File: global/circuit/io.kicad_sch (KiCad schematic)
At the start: 15 parts

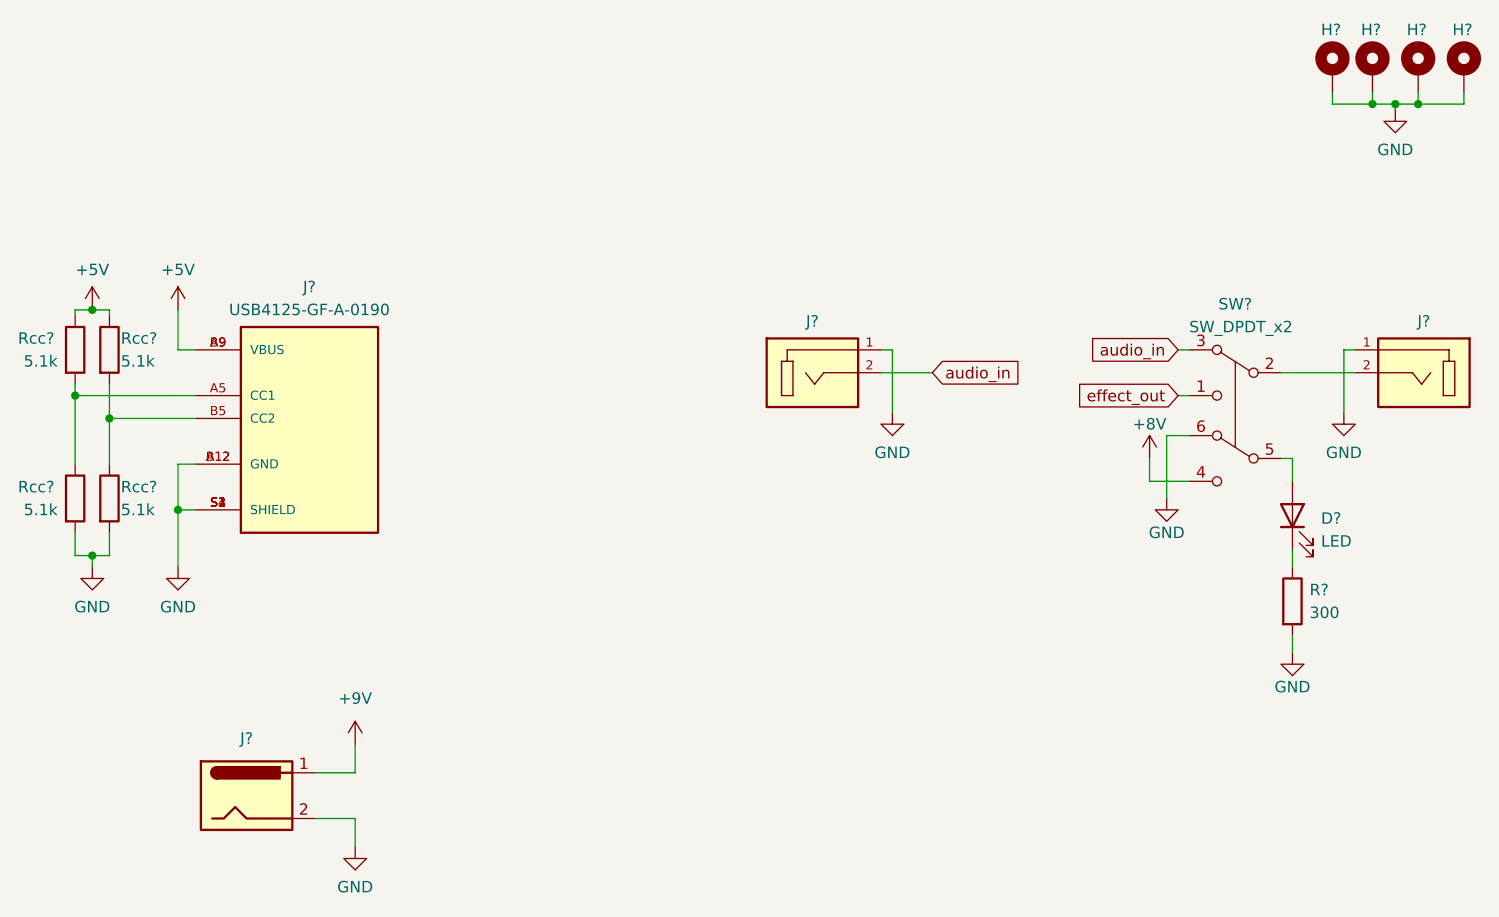
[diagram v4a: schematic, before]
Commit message: minor circuit rework for better use with multiple projects
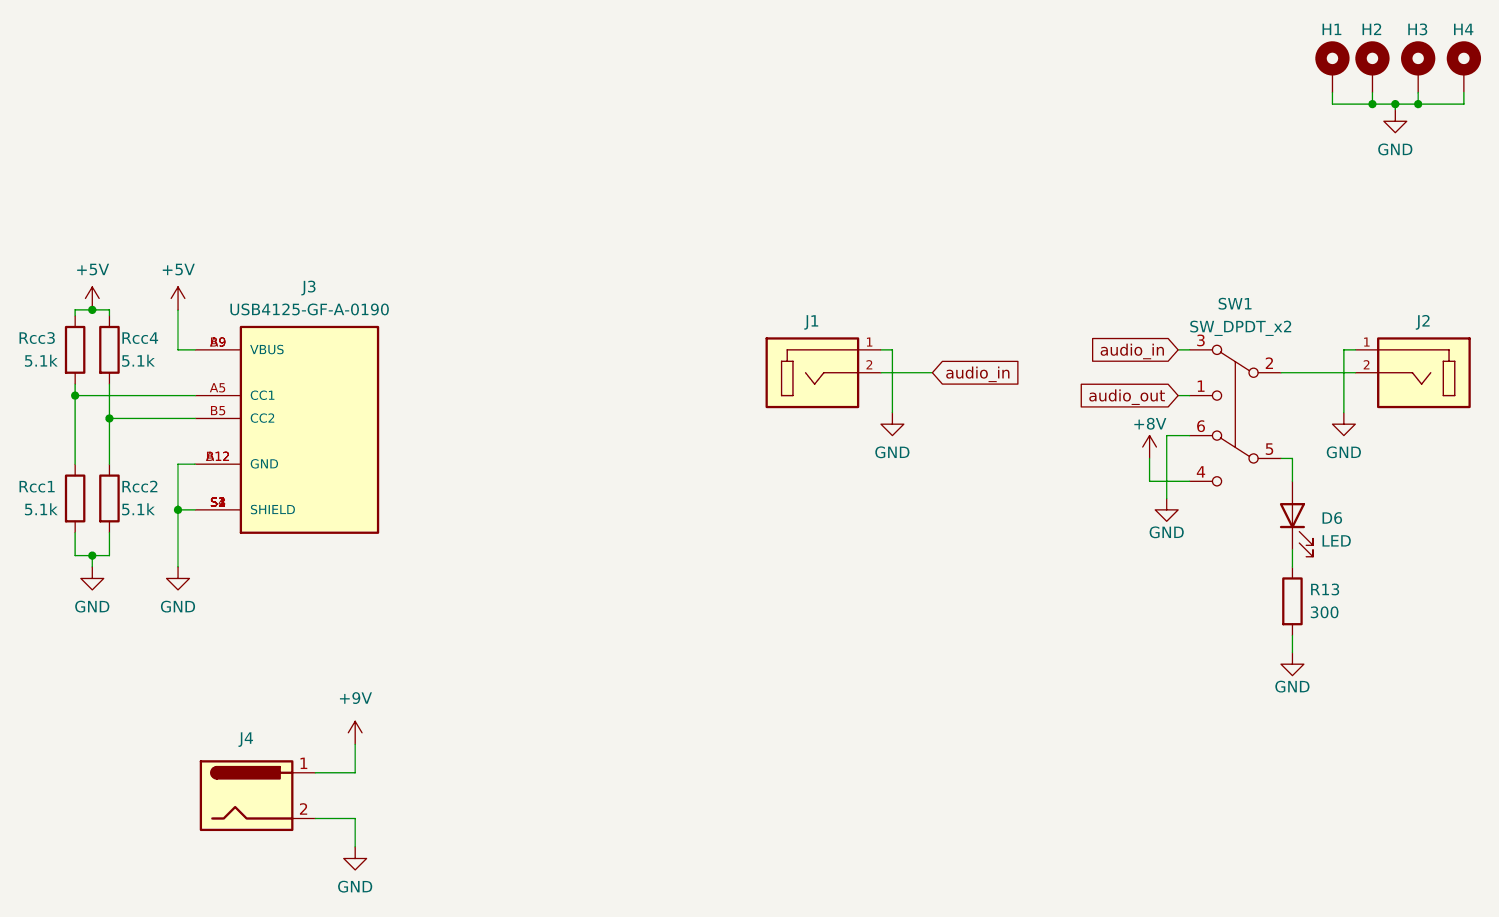
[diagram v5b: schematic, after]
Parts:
- J2: renamed from J?; footprint effect_pedal:audio_jack_wired -> effect_pedal:audio_jack_wired_shield_only
- J4: renamed from J?; footprint effect_pedal:barrel_jack_wired -> Connector_PinHeader_2.54mm:PinHeader_1x02_P2.54mm_Vertical
- SW1: renamed from SW?; footprint effect_pedal:switch_wired -> effect_pedal:switch_wired_reduced
- gave numbers to parts that had none: 12
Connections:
- net effect_out renamed audio_out
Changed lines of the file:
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@@
     )
   )
-  (global_label "effect_out" (shape input) (at 151.765 58.42 180) (fields_autoplaced)
+  (global_label "audio_out" (shape input) (at 151.765 58.42 180) (fields_autoplaced)
     (effects (font (size 1.27 1.27)) (justify right))
-    (property "Intersheet References" "${INTERSHEET_REFS}" (id 0) (at 139.9176 58.3406 0)
+    (property "Intersheet References" "${INTERSHEET_REFS}" (id 0) (at 140.1595 58.3406 0)
       (effects (font (size 1.27 1.27)) (justify right) hide)
     )
@@
   (symbol (lib_id "power:GND") (at 120.015 60.325 0) (unit 1)
     (in_bom yes) (on_board yes)
-    (property "Reference" "#PWR?" (id 0) (at 120.015 66.675 0)
+    (property "Reference" "#PWR0109" (id 0) (at 120.015 66.675 0)
       (effects (font (size 1.27 1.27)) hide)
     )
@@
   (symbol (lib_id "power:GND") (at 150.495 69.85 0) (unit 1)
     (in_bom yes) (on_board yes)
-    (property "Reference" "#PWR?" (id 0) (at 150.495 76.2 0)
+    (property "Reference" "#PWR026" (id 0) (at 150.495 76.2 0)
       (effects (font (size 1.27 1.27)) hide)
     )
@@
   (symbol (lib_id "power:+5V") (at 31.115 48.895 0) (unit 1)
     (in_bom yes) (on_board yes)
-    (property "Reference" "#PWR?" (id 0) (at 31.115 52.705 0)
+    (property "Reference" "#PWR028" (id 0) (at 31.115 52.705 0)
       (effects (font (size 1.27 1.27)) hide)
     )
@@
   (symbol (lib_id "Connector:Barrel_Jack") (at 48.26 102.87 0) (unit 1)
     (in_bom yes) (on_board yes)
-    (property "Reference" "J?" (id 0) (at 48.26 96.52 0))
+    (property "Reference" "J4" (id 0) (at 48.26 96.52 0))
     (property "Value" "Barrel_Jack" (id 1) (at 48.26 96.52 0)
       (effects (font (size 1.27 1.27)) hide)
     )
-    (property "Footprint" "effect_pedal:barrel_jack_wired" (id 2) (at 49.53 103.886 0)
+    (property "Footprint" "Connector_PinHeader_2.54mm:PinHeader_1x02_P2.54mm_Vertical" (id 2) (at 49.53 103.886 0)
       (effects (font (size 1.27 1.27)) hide)
     )
@@
   (symbol (lib_id "Device:R") (at 33.02 53.34 0) (unit 1)
     (in_bom yes) (on_board yes)
-    (property "Reference" "Rcc?" (id 0) (at 34.29 52.07 0)
+    (property "Reference" "Rcc4" (id 0) (at 34.29 52.07 0)
       (effects (font (size 1.27 1.27)) (justify left))
     )
@@
   (symbol (lib_id "power:GND") (at 40.64 77.47 0) (unit 1)
     (in_bom yes) (on_board yes)
-    (property "Reference" "#PWR?" (id 0) (at 40.64 83.82 0)
+    (property "Reference" "#PWR0113" (id 0) (at 40.64 83.82 0)
       (effects (font (size 1.27 1.27)) hide)
     )
@@
   (symbol (lib_id "power:+9V") (at 60.325 97.155 0) (unit 1)
     (in_bom yes) (on_board yes) (fields_autoplaced)
-    (property "Reference" "#PWR?" (id 0) (at 60.325 100.965 0)
+    (property "Reference" "#PWR0101" (id 0) (at 60.325 100.965 0)
       (effects (font (size 1.27 1.27)) hide)
     )
@@
   (symbol (lib_id "Mechanical:MountingHole_Pad") (at 178.435 22.225 0) (unit 1)
     (in_bom yes) (on_board yes)
-    (property "Reference" "H?" (id 0) (at 177.165 17.78 0)
+    (property "Reference" "H3" (id 0) (at 177.165 17.78 0)
       (effects (font (size 1.27 1.27)) (justify left))
     )
@@
   (symbol (lib_id "power:GND") (at 170.18 60.325 0) (unit 1)
     (in_bom yes) (on_board yes)
-    (property "Reference" "#PWR?" (id 0) (at 170.18 66.675 0)
+    (property "Reference" "#PWR0108" (id 0) (at 170.18 66.675 0)
       (effects (font (size 1.27 1.27)) hide)
     )
@@
   (symbol (lib_id "Device:R") (at 164.465 81.28 0) (unit 1)
     (in_bom yes) (on_board yes) (fields_autoplaced)
-    (property "Reference" "R?" (id 0) (at 166.37 80.0099 0)
+    (property "Reference" "R13" (id 0) (at 166.37 80.0099 0)
       (effects (font (size 1.27 1.27)) (justify left))
     )
@@
   (symbol (lib_id "Mechanical:MountingHole_Pad") (at 183.515 22.225 0) (unit 1)
     (in_bom yes) (on_board yes)
-    (property "Reference" "H?" (id 0) (at 182.245 17.78 0)
+    (property "Reference" "H4" (id 0) (at 182.245 17.78 0)
       (effects (font (size 1.27 1.27)) (justify left))
     )
@@
   (symbol (lib_id "Device:R") (at 29.21 69.85 0) (unit 1)
     (in_bom yes) (on_board yes)
-    (property "Reference" "Rcc?" (id 0) (at 22.86 68.58 0)
+    (property "Reference" "Rcc1" (id 0) (at 22.86 68.58 0)
       (effects (font (size 1.27 1.27)) (justify left))
     )
@@
   (symbol (lib_id "power:+5V") (at 40.64 48.895 0) (unit 1)
     (in_bom yes) (on_board yes)
-    (property "Reference" "#PWR?" (id 0) (at 40.64 52.705 0)
+    (property "Reference" "#PWR0114" (id 0) (at 40.64 52.705 0)
       (effects (font (size 1.27 1.27)) hide)
     )
@@
   (symbol (lib_id "effect_pedal:audio_jack_1_GND") (at 111.125 55.88 0) (unit 1)
     (in_bom yes) (on_board yes)
-    (property "Reference" "J?" (id 0) (at 111.125 50.165 0))
+    (property "Reference" "J1" (id 0) (at 111.125 50.165 0))
     (property "Value" "AudioJack2_Ground" (id 1) (at 110.49 49.53 0)
       (effects (font (size 1.27 1.27)) hide)
@@
   (symbol (lib_id "effect_pedal:USB4125-GF-A-0190_REVA2") (at 55.245 60.96 0) (unit 1)
     (in_bom yes) (on_board yes)
-    (property "Reference" "J?" (id 0) (at 55.245 46.355 0))
+    (property "Reference" "J3" (id 0) (at 55.245 46.355 0))
     (property "Value" "USB4125-GF-A-0190" (id 1) (at 55.245 48.895 0))
     (property "Footprint" "GCT_USB4125-GF-A-0190_REVA2" (id 2) (at 55.245 60.96 0)
@@
   (symbol (lib_id "effect_pedal:audio_jack_1_GND") (at 179.07 55.88 0) (mirror y) (unit 1)
     (in_bom yes) (on_board yes)
-    (property "Reference" "J?" (id 0) (at 179.07 50.165 0))
+    (property "Reference" "J2" (id 0) (at 179.07 50.165 0))
     (property "Value" "AudioJack2_Ground" (id 1) (at 179.705 49.53 0)
       (effects (font (size 1.27 1.27)) hide)
     )
-    (property "Footprint" "effect_pedal:audio_jack_wired" (id 2) (at 179.07 55.88 0)
+    (property "Footprint" "effect_pedal:audio_jack_wired_shield_only" (id 2) (at 179.07 55.88 0)
       (effects (font (size 1.27 1.27)) hide)
     )
@@
   (symbol (lib_id "Mechanical:MountingHole_Pad") (at 168.91 22.225 0) (unit 1)
     (in_bom yes) (on_board yes)
-    (property "Reference" "H?" (id 0) (at 167.64 17.78 0)
+    (property "Reference" "H1" (id 0) (at 167.64 17.78 0)
       (effects (font (size 1.27 1.27)) (justify left))
     )
@@
   (symbol (lib_id "power:GND") (at 31.115 77.47 0) (unit 1)
     (in_bom yes) (on_board yes)
-    (property "Reference" "#PWR?" (id 0) (at 31.115 83.82 0)
+    (property "Reference" "#PWR0112" (id 0) (at 31.115 83.82 0)
       (effects (font (size 1.27 1.27)) hide)
     )
@@
   (symbol (lib_id "power:GND") (at 175.895 26.67 0) (unit 1)
     (in_bom yes) (on_board yes) (fields_autoplaced)
-    (property "Reference" "#PWR?" (id 0) (at 175.895 33.02 0)
+    (property "Reference" "#PWR05" (id 0) (at 175.895 33.02 0)
       (effects (font (size 1.27 1.27)) hide)
     )
@@
   (symbol (lib_id "effect_pedal:SF12011F-0202-20R-L-050") (at 160.02 55.88 0) (mirror y) (unit 1)
     (in_bom yes) (on_board yes)
-    (property "Reference" "SW?" (id 0) (at 158.115 48.26 0))
+    (property "Reference" "SW1" (id 0) (at 158.115 48.26 0))
     (property "Value" "SW_DPDT_x2" (id 1) (at 158.75 50.8 0))
-    (property "Footprint" "effect_pedal:switch_wired" (id 2) (at 133.35 53.34 0)
+    (property "Footprint" "effect_pedal:switch_wired_reduced" (id 2) (at 133.35 53.34 0)
       (effects (font (size 1.27 1.27)) (justify left) hide)
     )
@@
   (symbol (lib_id "power:GND") (at 60.325 108.585 0) (unit 1)
     (in_bom yes) (on_board yes) (fields_autoplaced)
-    (property "Reference" "#PWR?" (id 0) (at 60.325 114.935 0)
+    (property "Reference" "#PWR0105" (id 0) (at 60.325 114.935 0)
       (effects (font (size 1.27 1.27)) hide)
     )
@@
   (symbol (lib_id "power:GND") (at 164.465 86.995 0) (unit 1)
     (in_bom yes) (on_board yes)
-    (property "Reference" "#PWR?" (id 0) (at 164.465 93.345 0)
+    (property "Reference" "#PWR027" (id 0) (at 164.465 93.345 0)
       (effects (font (size 1.27 1.27)) hide)
     )
@@
   (symbol (lib_id "Device:LED") (at 164.465 71.755 90) (unit 1)
     (in_bom yes) (on_board yes) (fields_autoplaced)
-    (property "Reference" "D?" (id 0) (at 167.64 72.0724 90)
+    (property "Reference" "D6" (id 0) (at 167.64 72.0724 90)
       (effects (font (size 1.27 1.27)) (justify right))
     )
@@
   (symbol (lib_id "Mechanical:MountingHole_Pad") (at 173.355 22.225 0) (unit 1)
     (in_bom yes) (on_board yes)
-    (property "Reference" "H?" (id 0) (at 172.085 17.78 0)
+    (property "Reference" "H2" (id 0) (at 172.085 17.78 0)
       (effects (font (size 1.27 1.27)) (justify left))
     )
@@
   (symbol (lib_id "Device:R") (at 33.02 69.85 0) (unit 1)
     (in_bom yes) (on_board yes)
-    (property "Reference" "Rcc?" (id 0) (at 34.29 68.58 0)
+    (property "Reference" "Rcc2" (id 0) (at 34.29 68.58 0)
       (effects (font (size 1.27 1.27)) (justify left))
     )
@@
   (symbol (lib_id "Device:R") (at 29.21 53.34 0) (unit 1)
     (in_bom yes) (on_board yes)
-    (property "Reference" "Rcc?" (id 0) (at 22.86 52.07 0)
+    (property "Reference" "Rcc3" (id 0) (at 22.86 52.07 0)
       (effects (font (size 1.27 1.27)) (justify left))
     )
@@
   (symbol (lib_id "power:+8V") (at 148.59 65.405 0) (unit 1)
     (in_bom yes) (on_board yes)
-    (property "Reference" "#PWR?" (id 0) (at 148.59 69.215 0)
-      (effects (font (size 1.27 1.27)) hide)
-    )
+    (property "Reference" "#PWR025" (id 0) (at 148.59 69.215 0)
+      (effects (font (size 1.27 1.27)) hide)
+    )
